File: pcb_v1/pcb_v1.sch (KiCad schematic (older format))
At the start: 37 parts, among them J1 Conn_02x03_Odd_Even, J2 Conn_01x02, J3 Conn_01x04, J4 Conn_01x07, U1 tmp117, U2 tmp117, U3 tmp117, U4 tmp117, U5 TC78H651AFNG,EL_Dual_H-Bridge, U6 STM32L432KBUx, Y1 Crystal

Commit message: added cubeide code
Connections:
- net OUT1: no longer names the net of U5.12 (OUT1)
- net OUT2: no longer names the net of U5.11 (OUT2)
- net PA4: no longer names the net of U6.10 (PA4)
- net PA4: no longer U5.7 (IN2)
- net PA5: no longer names the net of U6.11 (PA5)
- net PA5: no longer U5.6 (IN1)
- no-connect marks 5 -> 22
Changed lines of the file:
@@
 	0    -1   -1   0
 $EndComp
-Text Label 6900 3350 0    50   ~ 0
-PA4
-Text Label 6900 3450 0    50   ~ 0
-PA5
-Text Label 6900 3550 0    50   ~ 0
-PA6
-Text Label 6900 3650 0    50   ~ 0
-PA7
-Text Label 8750 4550 2    50   ~ 0
-PA4
-Text Label 8750 4450 2    50   ~ 0
-PA5
-Text Label 8750 4250 2    50   ~ 0
-PA6
-Text Label 8750 4150 2    50   ~ 0
-PA7
 Text Label 9450 4050 0    50   ~ 0
 OUT4
 Text Label 9450 4150 0    50   ~ 0
 OUT3
-Text Label 9450 4450 0    50   ~ 0
-OUT2
-Text Label 9450 4350 0    50   ~ 0
-OUT1
 $Comp
 L power:GND #PWR020
@@
 Text Notes 8500 3700 0    50   ~ 0
 Heater
+NoConn ~ 6900 2950
+NoConn ~ 6900 3050
+NoConn ~ 6900 3750
+NoConn ~ 6900 4050
+NoConn ~ 6900 4150
+NoConn ~ 6900 4450
+NoConn ~ 5900 4250
+NoConn ~ 5900 4150
+NoConn ~ 5900 4050
+NoConn ~ 5900 3950
+NoConn ~ 5900 3850
+Text Label 8750 4250 2    50   ~ 0
+PA6
+Text Label 8750 4150 2    50   ~ 0
+PA7
+Text Label 6900 3650 0    50   ~ 0
+PA7
+Text Label 6900 3550 0    50   ~ 0
+PA6
+NoConn ~ 8750 4550
+NoConn ~ 8750 4450
+NoConn ~ 6900 3450
+NoConn ~ 6900 3350
+NoConn ~ 9450 4450
+NoConn ~ 9450 4350
 $EndSCHEMATC

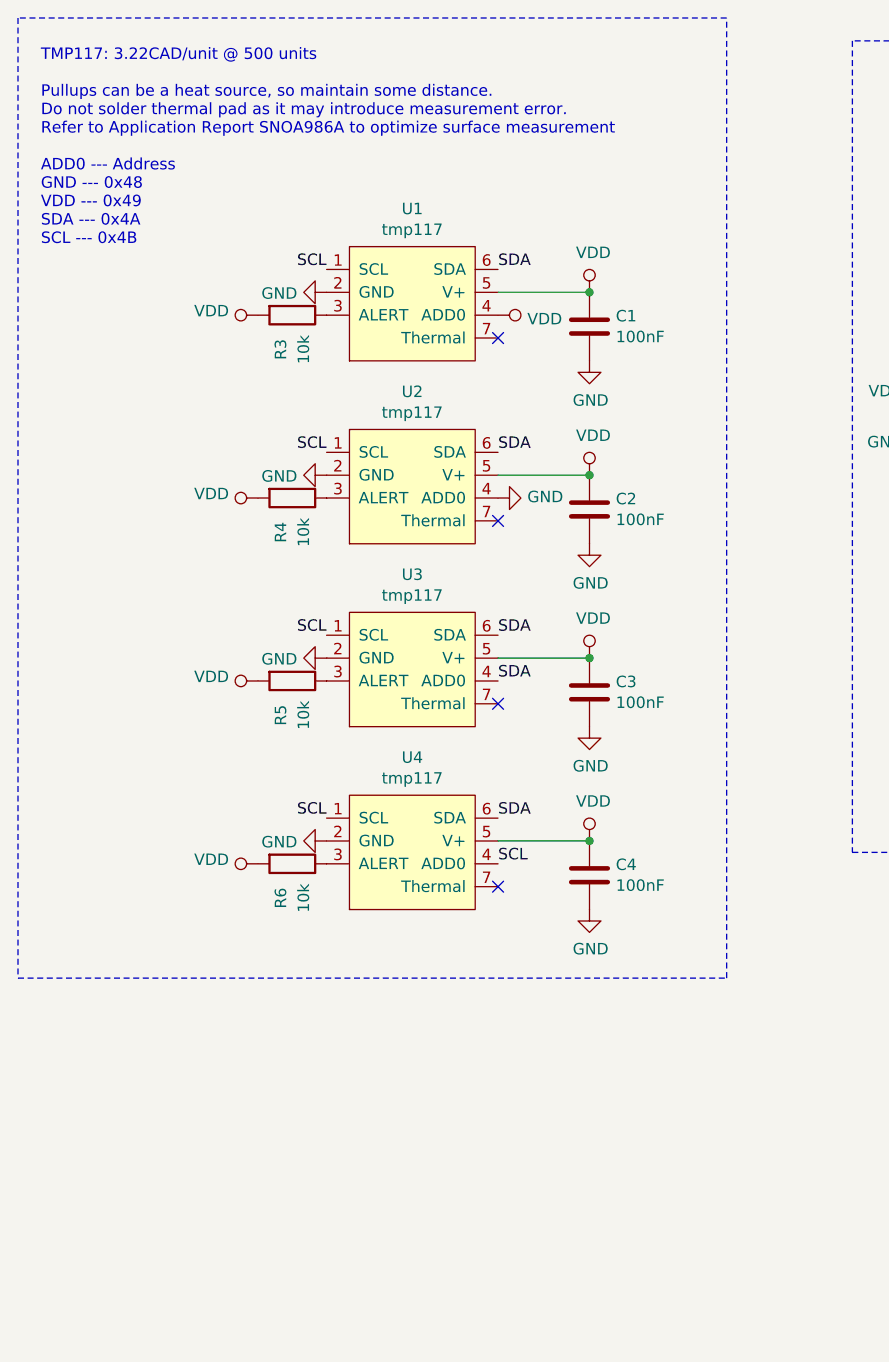
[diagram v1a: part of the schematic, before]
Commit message: Updated PCB w extra position
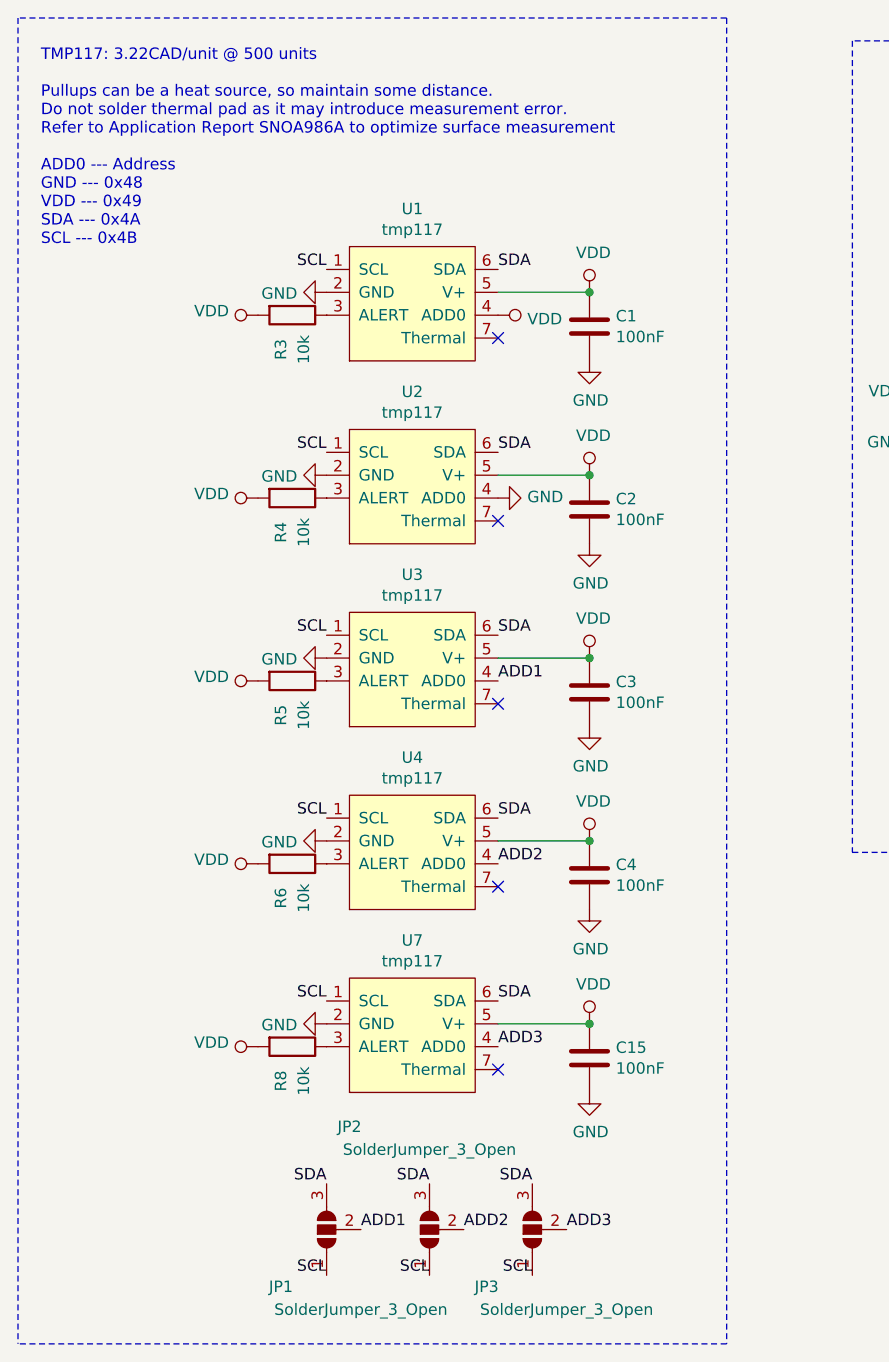
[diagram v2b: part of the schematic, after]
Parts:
- added C15: 100nF, Capacitor_SMD:C_0603_1608Metric, symbol Device:C
- added JP1, JP2, JP3: SolderJumper_3_Open, Jumper:SolderJumper-3_P1.3mm_Open_RoundedPad1.0x1.5mm_NumberLabels, symbol Jumper:SolderJumper_3_Open
- added R8: 10k, Capacitor_SMD:C_0603_1608Metric, symbol Device:R
- added U7: tmp117, Package_SON:WSON-6-1EP_2x2mm_P0.65mm_EP1x1.6mm, symbol flowsensor:tmp117
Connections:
- net GND: now also C15.1, U7.2 (GND)
- net SCL: now also JP1.1 (A), JP2.1 (A), JP3.1 (A), U7.1 (SCL); no longer U4.4 (ADD0)
- net SDA: now also JP1.3 (B), JP2.3 (B), JP3.3 (B), U7.6 (SDA); no longer U3.4 (ADD0)
- net VDD: now also C15.2, R8.2, U7.5 (V+)
- new net: R8.1, U7.3 (ALERT)
- new net ADD1: JP1.2 (C), U3.4 (ADD0)
- new net ADD2: JP2.2 (C), U4.4 (ADD0)
- new net ADD3: JP3.2 (C), U7.4 (ADD0)
- no-connect marks 22 -> 23
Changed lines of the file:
@@
 	0    -1   -1   0
 $EndComp
-Text Label 2900 4250 0    50   ~ 0
+Text Label 2150 6450 2    50   ~ 0
 SDA
-Text Label 2900 5050 0    50   ~ 0
+Text Label 2150 6850 2    50   ~ 0
 SCL
 Text Notes 900  2350 0    50   ~ 0
@@
 $EndComp
 Wire Notes Line
-	800  5550 3900 5550
-Wire Notes Line
-	3900 5550 3900 1350
-Wire Notes Line
 	3900 1350 800  1350
-Wire Notes Line
-	800  1350 800  5550
 Text Notes 4800 1650 0    50   ~ 0
 STM32L432KB MCU
@@
 NoConn ~ 9450 4450
 NoConn ~ 9450 4350
+$Comp
+L flowsensor:tmp117 U7
+U 1 1 61EAF2D8
+P 2250 6050
+F 0 "U7" H 2525 6715 50  0000 C CNN
+F 1 "tmp117" H 2525 6624 50  0000 C CNN
+F 2 "Package_SON:WSON-6-1EP_2x2mm_P0.65mm_EP1x1.6mm" H 2150 6250 50  0001 C CNN
+F 3 "" H 2150 6250 50  0001 C CNN
+	1    2250 6050
+	1    0    0    -1
+$EndComp
+$Comp
+L Device:R R8
+U 1 1 61EAF2DE
+P 2000 5850
+F 0 "R8" H 2150 5800 50  0000 C CNN
+F 1 "10k" H 2150 5900 50  0000 C CNN
+F 2 "Capacitor_SMD:C_0603_1608Metric" V 1930 5850 50  0001 C CNN
+F 3 "~" H 2000 5850 50  0001 C CNN
+	1    2000 5850
+	0    1    1    0
+$EndComp
+$Comp
+L power:VDD #PWR0103
+U 1 1 61EAF2E4
+P 1850 5850
+F 0 "#PWR0103" H 1850 5700 50  0001 C CNN
+F 1 "VDD" V 1868 5977 50  0000 L CNN
+F 2 "" H 1850 5850 50  0001 C CNN
+F 3 "" H 1850 5850 50  0001 C CNN
+	1    1850 5850
+	0    -1   -1   0
+$EndComp
+Text Label 2150 5650 2    50   ~ 0
+SCL
+$Comp
+L power:GND #PWR0104
+U 1 1 61EAF2EB
+P 2150 5750
+F 0 "#PWR0104" H 2150 5500 50  0001 C CNN
+F 1 "GND" V 2155 5622 50  0000 R CNN
+F 2 "" H 2150 5750 50  0001 C CNN
+F 3 "" H 2150 5750 50  0001 C CNN
+	1    2150 5750
+	0    1    1    0
+$EndComp
+Text Label 2900 5650 0    50   ~ 0
+SDA
+$Comp
+L power:VDD #PWR0108
+U 1 1 61EAF2F3
+P 3300 5750
+F 0 "#PWR0108" H 3300 5600 50  0001 C CNN
+F 1 "VDD" H 3317 5923 50  0000 C CNN
+F 2 "" H 3300 5750 50  0001 C CNN
+F 3 "" H 3300 5750 50  0001 C CNN
+	1    3300 5750
+	1    0    0    -1
+$EndComp
+$Comp
+L Device:C C15
+U 1 1 61EAF2F9
+P 3300 5900
+F 0 "C15" H 3185 5854 50  0000 R CNN
+F 1 "100nF" H 3185 5945 50  0000 R CNN
+F 2 "Capacitor_SMD:C_0603_1608Metric" H 3338 5750 50  0001 C CNN
+F 3 "~" H 3300 5900 50  0001 C CNN
+	1    3300 5900
+	-1   0    0    1
+$EndComp
+Wire Wire Line
+	3300 5750 2900 5750
+Connection ~ 3300 5750
+$Comp
+L power:GND #PWR0109
+U 1 1 61EAF301
+P 3300 6050
+F 0 "#PWR0109" H 3300 5800 50  0001 C CNN
+F 1 "GND" H 3305 5877 50  0000 C CNN
+F 2 "" H 3300 6050 50  0001 C CNN
+F 3 "" H 3300 6050 50  0001 C CNN
+	1    3300 6050
+	1    0    0    -1
+$EndComp
+NoConn ~ 2900 5950
+Text Label 2900 4250 0    50   ~ 0
+ADD1
+Text Label 2900 5050 0    50   ~ 0
+ADD2
+Text Label 2900 5850 0    50   ~ 0
+ADD3
+Text Label 2300 6650 0    50   ~ 0
+ADD1
+Text Label 2750 6650 0    50   ~ 0
+ADD2
+Text Label 3200 6650 0    50   ~ 0
+ADD3
+$Comp
+L Jumper:SolderJumper_3_Open JP1
+U 1 1 61F8FAC1
+P 2150 6650
+F 0 "JP1" V 1900 6850 50  0000 C CNN
+F 1 "SolderJumper_3_Open" V 1800 6500 50  0000 C CNN
+F 2 "Jumper:SolderJumper-3_P1.3mm_Open_RoundedPad1.0x1.5mm_NumberLabels" H 2150 6650 50  0001 C CNN
+F 3 "~" H 2150 6650 50  0001 C CNN
+	1    2150 6650
+	0    -1   -1   0
+$EndComp
+Text Label 2600 6450 2    50   ~ 0
+SDA
+Text Label 2600 6850 2    50   ~ 0
+SCL
+$Comp
+L Jumper:SolderJumper_3_Open JP2
+U 1 1 61F987D5
+P 2600 6650
+F 0 "JP2" V 3050 7000 50  0000 C CNN
+F 1 "SolderJumper_3_Open" V 2950 6650 50  0000 C CNN
+F 2 "Jumper:SolderJumper-3_P1.3mm_Open_RoundedPad1.0x1.5mm_NumberLabels" H 2600 6650 50  0001 C CNN
+F 3 "~" H 2600 6650 50  0001 C CNN
+	1    2600 6650
+	0    -1   -1   0
+$EndComp
+Text Label 3050 6450 2    50   ~ 0
+SDA
+Text Label 3050 6850 2    50   ~ 0
+SCL
+$Comp
+L Jumper:SolderJumper_3_Open JP3
+U 1 1 61F9B9B4
+P 3050 6650
+F 0 "JP3" V 2800 6850 50  0000 C CNN
+F 1 "SolderJumper_3_Open" V 2700 6500 50  0000 C CNN
+F 2 "Jumper:SolderJumper-3_P1.3mm_Open_RoundedPad1.0x1.5mm_NumberLabels" H 3050 6650 50  0001 C CNN
+F 3 "~" H 3050 6650 50  0001 C CNN
+	1    3050 6650
+	0    -1   -1   0
+$EndComp
+Wire Notes Line
+	3900 7150 800  7150
+Wire Notes Line
+	3900 1350 3900 7150
+Wire Notes Line
+	800  1350 800  7150
 $EndSCHEMATC

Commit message: updated PCB files
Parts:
- U1, U2, U3, U4, U7: footprint Package_SON:WSON-6-1EP_2x2mm_P0.65mm_EP1x1.6mm -> flowsensor:THERMAL_ENHANCED_WSON-6-1EP_2x2mm_P0.65mm_EP1x1.6mm
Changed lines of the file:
@@
 F 0 "U1" H 2525 3515 50  0000 C CNN
 F 1 "tmp117" H 2525 3424 50  0000 C CNN
-F 2 "Package_SON:WSON-6-1EP_2x2mm_P0.65mm_EP1x1.6mm" H 2150 3050 50  0001 C CNN
+F 2 "flowsensor:THERMAL_ENHANCED_WSON-6-1EP_2x2mm_P0.65mm_EP1x1.6mm" H 2150 3050 50  0001 C CNN
 F 3 "" H 2150 3050 50  0001 C CNN
 	1    2250 2850
@@
 F 0 "U3" H 2525 5115 50  0000 C CNN
 F 1 "tmp117" H 2525 5024 50  0000 C CNN
-F 2 "Package_SON:WSON-6-1EP_2x2mm_P0.65mm_EP1x1.6mm" H 2150 4650 50  0001 C CNN
+F 2 "flowsensor:THERMAL_ENHANCED_WSON-6-1EP_2x2mm_P0.65mm_EP1x1.6mm" H 2150 4650 50  0001 C CNN
 F 3 "" H 2150 4650 50  0001 C CNN
 	1    2250 4450
@@
 F 0 "U2" H 2525 4315 50  0000 C CNN
 F 1 "tmp117" H 2525 4224 50  0000 C CNN
-F 2 "Package_SON:WSON-6-1EP_2x2mm_P0.65mm_EP1x1.6mm" H 2150 3850 50  0001 C CNN
+F 2 "flowsensor:THERMAL_ENHANCED_WSON-6-1EP_2x2mm_P0.65mm_EP1x1.6mm" H 2150 3850 50  0001 C CNN
 F 3 "" H 2150 3850 50  0001 C CNN
 	1    2250 3650
@@
 F 0 "U4" H 2525 5915 50  0000 C CNN
 F 1 "tmp117" H 2525 5824 50  0000 C CNN
-F 2 "Package_SON:WSON-6-1EP_2x2mm_P0.65mm_EP1x1.6mm" H 2150 5450 50  0001 C CNN
+F 2 "flowsensor:THERMAL_ENHANCED_WSON-6-1EP_2x2mm_P0.65mm_EP1x1.6mm" H 2150 5450 50  0001 C CNN
 F 3 "" H 2150 5450 50  0001 C CNN
 	1    2250 5250
@@
 F 0 "U7" H 2525 6715 50  0000 C CNN
 F 1 "tmp117" H 2525 6624 50  0000 C CNN
-F 2 "Package_SON:WSON-6-1EP_2x2mm_P0.65mm_EP1x1.6mm" H 2150 6250 50  0001 C CNN
+F 2 "flowsensor:THERMAL_ENHANCED_WSON-6-1EP_2x2mm_P0.65mm_EP1x1.6mm" H 2150 6250 50  0001 C CNN
 F 3 "" H 2150 6250 50  0001 C CNN
 	1    2250 6050
